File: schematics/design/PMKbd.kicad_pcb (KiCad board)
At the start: 2 copper layers, 28.4 x 53 mm, 84 parts, among them J1 Conn_01x01, J10 Conn_01x01, J11 Conn_01x01, J12 Conn_01x01, J13 Conn_01x01, J14 Conn_01x01, J15 Conn_01x01, J16 Conn_01x01, J17 Conn_01x01, J18 Conn_01x01, J19 Conn_01x01, J2 Conn_01x01, J20 Conn_01x01, J21 Conn_01x01, J22 Conn_01x01, J23 Conn_01x01, J24 Conn_01x01, J25 Conn_01x01, J26 Conn_01x01, J27 Conn_01x01, J28 Conn_01x01, J29 Conn_01x01, J3 Conn_01x01, J30 Conn_01x01, J31 Conn_01x01, J32 Conn_01x01, J33 Conn_01x01, J34 Conn_01x01, J35 Conn_01x01, J36 Conn_01x01, J37 Conn_01x01, J38 Conn_01x01, J39 Conn_01x01, J4 Conn_01x01, J40 Conn_01x01, J41 Conn_01x01, J42 Conn_01x01, J43 Conn_01x01, J44 Conn_01x01, J45 Conn_01x01, J46 Conn_01x01, J47 Conn_01x01, J48 Conn_01x01, J49 Conn_01x01, J5 Conn_01x01, J50 Conn_01x01, J51 Conn_01x01, J52 Conn_01x01, J53 Conn_01x01, J54 Conn_01x01, J55 Conn_01x01, J56 Conn_01x01, J57 Conn_01x01, J58 Conn_01x01, J59 Conn_01x01, J6 Conn_01x01, J60 Conn_01x01, J61 Conn_01x01, J62 Conn_01x01, J63 Conn_01x01, J64 Conn_01x01, J65 Conn_01x01, J66 Conn_01x01, J7 Conn_01x01, J8 Conn_01x01, J9 Conn_01x01, Q1 2N2222, Q2 2N2222, U1 Core51822_(B), U2 LT1117-3.3, U3 MCP73831-2-OT, U4 Core51822_(B), U5 MCP73831-2-OT, U6 LT1117-3.3

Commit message: fixed references
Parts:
- added J67: Conn_01x01, Connector_Wire:SolderWirePad_1x01_SMD_1x2mm, B.Cu at (151.8, 15.4)
- added J68: Conn_01x01, Connector_Wire:SolderWirePad_1x01_SMD_1x2mm, B.Cu at (162.8, 29.6)
- added J69: Conn_01x01, Connector_Wire:SolderWirePad_1x01_SMD_1x2mm, B.Cu at (153.0, 11.8)
- added J70: Conn_01x01, Connector_Wire:SolderWirePad_1x01_SMD_1x2mm, B.Cu at (172.3, 10.7)
- added J71: Conn_01x01, Connector_Wire:SolderWirePad_1x01_SMD_1x2mm, B.Cu at (150.7, 9.84)
- added J72: Conn_01x01, Connector_Wire:SolderWirePad_1x01_SMD_1x2mm, B.Cu at (168.0, 18.4)
- added J73: Conn_01x01, Connector_Wire:SolderWirePad_1x01_SMD_1x2mm, B.Cu at (173.2, 35.1)
- added J74: Conn_01x01, Connector_Wire:SolderWirePad_1x01_SMD_1x2mm, B.Cu at (166.9, 34.7)
- J34, J35, J36, J37: moved to F.Cu
- R10: value 200 -> 10K
- R9: value 10K -> 200
- U5: value MCP73831-2-OT -> LT1117-3.3
- U6: value LT1117-3.3 -> MCP73831-2-OT
- moved J35 76.6 mm to (100.4, 85.6)
- moved J37 73.1 mm to (99.5, 79.1)
- moved J36 72.1 mm to (102.7, 82.7)
- moved J34 71.0 mm to (97.7, 84.7)
- moved U4 52.3 mm to (75.3, 12.6)
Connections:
- net +5V renamed 5V_L
- net 3.3V renamed 3.3V_L
- net GND renamed GND_L
- net LED renamed LED_L
- J34 pad 1: Net-(J34-Pad1) -> EXT1
- J35 pad 1: Net-(J35-Pad1) -> EXT2
- J36 pad 1: Net-(BT2-Pad1) -> EXT3
- J37 pad 1: GND_R -> EXT4
- J40 pad 1: GND_R -> S24
- J41 pad 1: GND_R -> S25
- J42 pad 1: GND_R -> S26
- J43 pad 1: GND_R -> S27
- J44 pad 1: S24 -> S28
- J45 pad 1: S25 -> S29
- J46 pad 1: S26 -> S30
- J47 pad 1: S27 -> S31
- J48 pad 1: S28 -> S32
- J49 pad 1: S29 -> S33
- J50 pad 1: S30 -> S34
- J51 pad 1: S31 -> S35
- J52 pad 1: S32 -> S36
- J53 pad 1: S33 -> S37
- J54 pad 1: S34 -> S38
- J55 pad 1: S35 -> S39
- J56 pad 1: S36 -> S40
- J57 pad 1: S37 -> S41
- J58 pad 1: S38 -> S42
- J59 pad 1: S39 -> S43
- J60 pad 1: S40 -> S44
- J61 pad 1: S41 -> S45
- J62 pad 1: S42 -> S46
- J63 pad 1: S43 -> Net-(BT2-Pad1)
- J64 pad 1: S44 -> GND_R
- J65 pad 1: S45 -> GND_R
- J66 pad 1: S46 -> Net-(J66-Pad1)
- R10 pad 1: Net-(J38-Pad1) -> LED_R
- R10 pad 2: 3.3V_R -> Net-(Q2-Pad2)
- R9 pad 1: LED_R -> Net-(J38-Pad1)
- R9 pad 2: Net-(Q2-Pad2) -> 3.3V_R
- U1 pad 26: Net-(U1-Pad26) -> EXT4
- U1 pad 3: Net-(U1-Pad3) -> EXT1
- U1 pad 4: Net-(U1-Pad4) -> EXT2
- U1 pad 6: Net-(U1-Pad6) -> EXT3
- U4 pad 26: Net-(U4-Pad26) -> EXT8
- U4 pad 3: Net-(U4-Pad3) -> EXT5
- U4 pad 31: Net-(J35-Pad1) -> Net-(J67-Pad1)
- U4 pad 32: Net-(J34-Pad1) -> Net-(J66-Pad1)
- U4 pad 4: Net-(U4-Pad4) -> EXT6
- U4 pad 6: Net-(U4-Pad6) -> EXT7
- U5 pad 1: Net-(R6-Pad2) -> GND_R
- U5 pad 2: GND_R -> 3.3V_R
- U5 pad 4: 5V_R -> (no net)
- U5 pad 5: Net-(R8-Pad2) -> (no net)
- U6 pad 1: GND_R -> Net-(R6-Pad2)
- U6 pad 2: 3.3V_R -> GND_R
- U6 pad 4: (no net) -> 5V_R

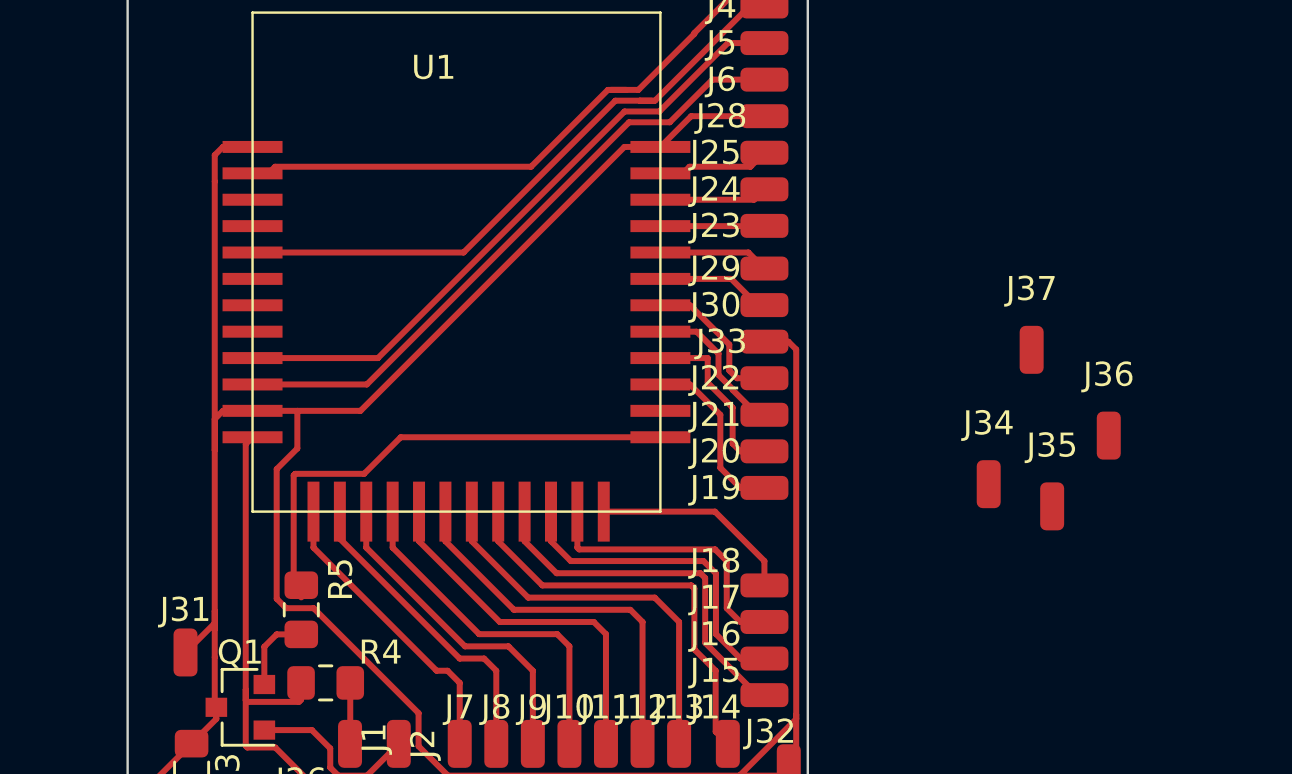
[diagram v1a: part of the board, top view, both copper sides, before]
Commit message: added EXT pads
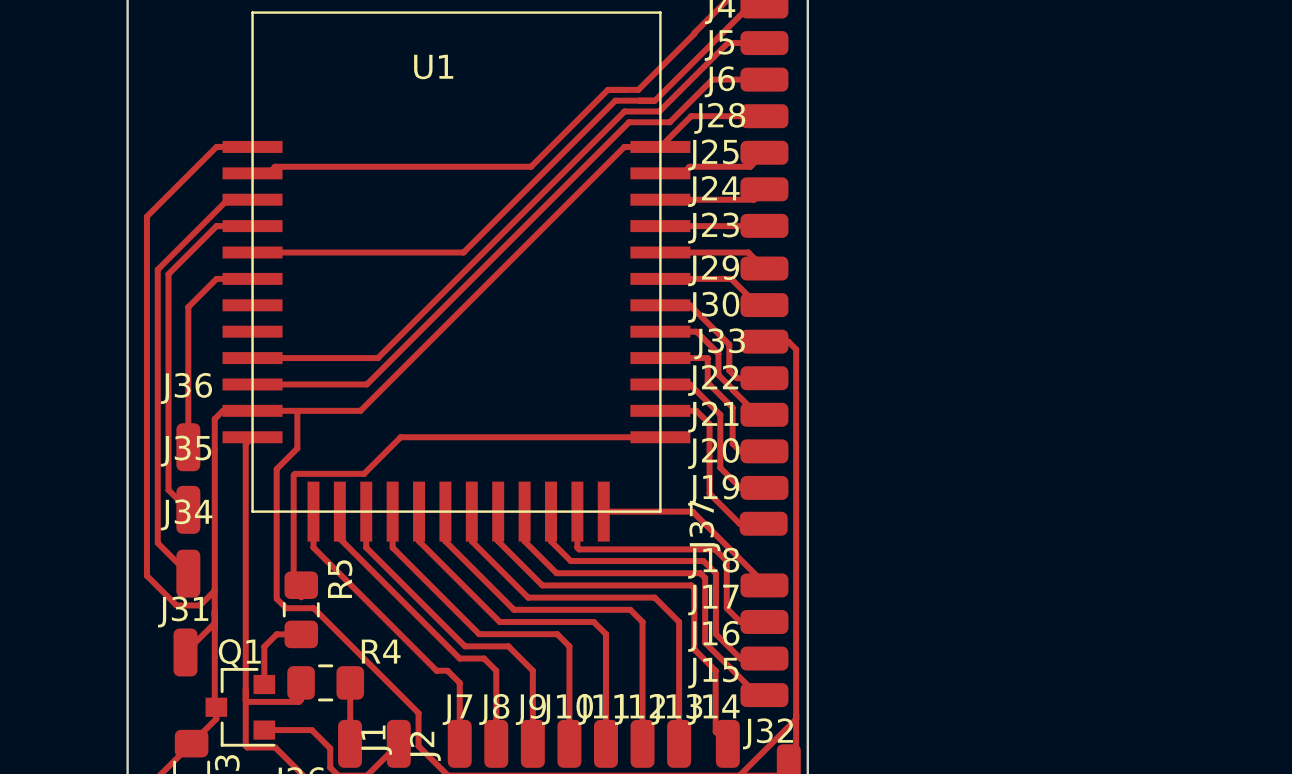
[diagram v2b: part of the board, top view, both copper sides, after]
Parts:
- moved J36 38.4 mm to (64.4, 83.1)
- moved J35 36.0 mm to (64.4, 85.8)
- moved J34 33.6 mm to (64.4, 88.4)
- moved J37 13.3 mm to (88.4, 86.3), turned to 90 degrees
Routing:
- net EXT1: track 0.00 -> 18.4 mm
- net EXT2: track 0.00 -> 14.5 mm
- net GND_L: track 145.0 -> 155.4 mm
- net EXT3: track 0.00 -> 9.00 mm
- net EXT4: track 0.00 -> 7.95 mm
- net S16: track 8.57 -> 8.02 mm
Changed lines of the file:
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@@
     (thickness 1.6)
     (drawings 6)
-    (tracks 243)
+    (tracks 264)
     (zones 0)
     (modules 92)
@@
   )
   (module Connector_Wire:SolderWirePad_1x01_SMD_1x2mm (layer F.Cu)
-    (at 99.53 79.08)
+    (at 88.36 86.33 90)
     (descr "Wire Pad, Square, SMD Pad,  5mm x 10mm,")
     (tags "MesurementPoint Square SMDPad 5mmx10mm ")
     (attr virtual)
-    (fp_text reference J37 (at 0 -2.54) (layer F.SilkS)
+    (fp_text reference J37 (at 0 -2.54 90) (layer F.SilkS)
       (effects (font (size 1 1) (thickness 0.15)))
     )
-    (fp_text value Conn_01x01 (at 0 2.54) (layer F.Fab)
+    (fp_text value Conn_01x01 (at 0 2.54 90) (layer F.Fab)
       (effects (font (size 1 1) (thickness 0.15)))
     )
@@
     (fp_line (start 0.63 1.27) (end 0.63 -1.27) (layer F.CrtYd) (width 0.05))
     (fp_line (start 0.63 -1.27) (end -0.63 -1.27) (layer F.CrtYd) (width 0.05))
-    (fp_text user %R (at 0 0) (layer F.Fab)
+    (fp_text user %R (at 0 0 90) (layer F.Fab)
       (effects (font (size 1 1) (thickness 0.15)))
     )
-    (pad 1 smd roundrect (at 0 0) (size 1 2) (layers F.Cu F.Paste F.Mask) (roundrect_rratio 0.25)
+    (pad 1 smd roundrect (at 0 0 90) (size 1 2) (layers F.Cu F.Paste F.Mask) (roundrect_rratio 0.25)
       (net 74 EXT4))
   )
   (module Connector_Wire:SolderWirePad_1x01_SMD_1x2mm (layer F.Cu)
-    (at 102.745 82.655)
+    (at 64.38 83.14)
     (descr "Wire Pad, Square, SMD Pad,  5mm x 10mm,")
     (tags "MesurementPoint Square SMDPad 5mmx10mm ")
@@
   )
   (module Connector_Wire:SolderWirePad_1x01_SMD_1x2mm (layer F.Cu)
-    (at 100.385 85.605)
+    (at 64.38 85.75)
     (descr "Wire Pad, Square, SMD Pad,  5mm x 10mm,")
     (tags "MesurementPoint Square SMDPad 5mmx10mm ")
@@
   )
   (module Connector_Wire:SolderWirePad_1x01_SMD_1x2mm (layer F.Cu)
-    (at 97.74 84.68)
+    (at 64.38 88.41)
     (descr "Wire Pad, Square, SMD Pad,  5mm x 10mm,")
     (tags "MesurementPoint Square SMDPad 5mmx10mm ")
@@
   (segment (start 65.820998 81.624) (end 65.480999 81.963999) (width 0.25) (layer F.Cu) (net 69))
   (segment (start 67.056 81.624) (end 65.820998 81.624) (width 0.25) (layer F.Cu) (net 69))
-  (segment (start 65.480999 70.963999) (end 65.480999 72.063999) (width 0.25) (layer F.Cu) (net 69))
-  (segment (start 67.056 70.624) (end 65.820998 70.624) (width 0.25) (layer F.Cu) (net 69))
-  (segment (start 65.820998 70.624) (end 65.480999 70.963999) (width 0.25) (layer F.Cu) (net 69))
   (segment (start 65.480999 81.963999) (end 65.480999 83.260999) (width 0.25) (layer F.Cu) (net 69))
-  (segment (start 65.480999 72.063999) (end 65.480999 83.260999) (width 0.25) (layer F.Cu) (net 69))
   (segment (start 65.548 94.463) (end 64.516 95.495) (width 0.25) (layer F.Cu) (net 69))
   (segment (start 65.548 93.98) (end 65.548 94.463) (width 0.25) (layer F.Cu) (net 69))
@@
   (segment (start 65.480999 90.626999) (end 65.480999 91.896999) (width 0.25) (layer F.Cu) (net 69))
   (segment (start 64.262 91.694) (end 65.480999 90.475001) (width 0.25) (layer F.Cu) (net 69))
-  (segment (start 65.480999 83.260999) (end 65.480999 89.967001) (width 0.25) (layer F.Cu) (net 69))
   (segment (start 65.480999 90.475001) (end 65.480999 89.967001) (width 0.25) (layer F.Cu) (net 69))
-  (segment (start 65.480999 89.967001) (end 65.480999 90.626999) (width 0.25) (layer F.Cu) (net 69))
   (segment (start 63.076999 102.192999) (end 63.076999 103.462999) (width 0.25) (layer F.Cu) (net 69))
   (segment (start 63.076999 103.462999) (end 62.156999 104.382999) (width 0.25) (layer F.Cu) (net 69))
@@
   (segment (start 88.382 73.924) (end 88.392 73.914) (width 0.25) (layer F.Cu) (net 25))
   (segment (start 84.056 73.924) (end 88.382 73.924) (width 0.25) (layer F.Cu) (net 25))
-  (segment (start 81.696 85.824) (end 86.332 85.824) (width 0.25) (layer F.Cu) (net 26))
-  (segment (start 88.392 87.884) (end 88.392 88.9) (width 0.25) (layer F.Cu) (net 26))
-  (segment (start 86.332 85.824) (end 88.392 87.884) (width 0.25) (layer F.Cu) (net 26))
+  (segment (start 88.392 88.817592) (end 88.392 88.9) (width 0.25) (layer F.Cu) (net 26))
+  (segment (start 85.398408 85.824) (end 88.392 88.817592) (width 0.25) (layer F.Cu) (net 26))
+  (segment (start 81.696 85.824) (end 85.398408 85.824) (width 0.25) (layer F.Cu) (net 26))
   (segment (start 85.291002 77.224) (end 84.056 77.224) (width 0.25) (layer F.Cu) (net 27))
   (segment (start 86.928019 78.861017) (end 85.291002 77.224) (width 0.25) (layer F.Cu) (net 27))
@@
   (segment (start 87.01081 76.124) (end 88.10281 77.216) (width 0.25) (layer F.Cu) (net 33))
   (segment (start 84.056 76.124) (end 87.01081 76.124) (width 0.25) (layer F.Cu) (net 33))
+  (segment (start 65.480999 89.967001) (end 65.480999 90.150999) (width 0.25) (layer F.Cu) (net 69))
+  (segment (start 65.480999 90.150999) (end 65.480999 90.626999) (width 0.25) (layer F.Cu) (net 69))
+  (segment (start 65.480999 89.122191) (end 65.480999 89.040999) (width 0.25) (layer F.Cu) (net 69))
+  (segment (start 64.86818 89.73501) (end 65.480999 89.122191) (width 0.25) (layer F.Cu) (net 69))
+  (segment (start 62.654971 73.525029) (end 62.654971 88.498161) (width 0.25) (layer F.Cu) (net 69))
+  (segment (start 63.89182 89.73501) (end 64.86818 89.73501) (width 0.25) (layer F.Cu) (net 69))
+  (segment (start 62.654971 88.498161) (end 63.89182 89.73501) (width 0.25) (layer F.Cu) (net 69))
+  (segment (start 65.556 70.624) (end 62.654971 73.525029) (width 0.25) (layer F.Cu) (net 69))
+  (segment (start 67.056 70.624) (end 65.556 70.624) (width 0.25) (layer F.Cu) (net 69))
+  (segment (start 65.480999 89.040999) (end 65.480999 90.150999) (width 0.25) (layer F.Cu) (net 69))
+  (segment (start 65.480999 83.260999) (end 65.480999 89.040999) (width 0.25) (layer F.Cu) (net 69))
+  (segment (start 63.10498 87.13498) (end 64.38 88.41) (width 0.25) (layer F.Cu) (net 71))
+  (segment (start 63.10498 75.73861) (end 63.10498 87.13498) (width 0.25) (layer F.Cu) (net 71))
+  (segment (start 66.01959 72.824) (end 63.10498 75.73861) (width 0.25) (layer F.Cu) (net 71))
+  (segment (start 67.056 72.824) (end 66.01959 72.824) (width 0.25) (layer F.Cu) (net 71))
+  (segment (start 63.55499 84.92499) (end 64.38 85.75) (width 0.25) (layer F.Cu) (net 72))
+  (segment (start 65.556 73.924) (end 63.55499 75.92501) (width 0.25) (layer F.Cu) (net 72))
+  (segment (start 63.55499 75.92501) (end 63.55499 84.92499) (width 0.25) (layer F.Cu) (net 72))
+  (segment (start 67.056 73.924) (end 65.556 73.924) (width 0.25) (layer F.Cu) (net 72))
+  (segment (start 65.556 76.124) (end 64.38 77.3) (width 0.25) (layer F.Cu) (net 73))
+  (segment (start 64.38 77.3) (end 64.38 83.14) (width 0.25) (layer F.Cu) (net 73))
+  (segment (start 67.056 76.124) (end 65.556 76.124) (width 0.25) (layer F.Cu) (net 73))
+  (segment (start 87.36 86.33) (end 88.36 86.33) (width 0.25) (layer F.Cu) (net 74))
+  (segment (start 86.104992 85.074992) (end 87.36 86.33) (width 0.25) (layer F.Cu) (net 74))
+  (segment (start 86.104992 82.172992) (end 86.104992 85.074992) (width 0.25) (layer F.Cu) (net 74))
+  (segment (start 85.556 81.624) (end 86.104992 82.172992) (width 0.25) (layer F.Cu) (net 74))
+  (segment (start 84.056 81.624) (end 85.556 81.624) (width 0.25) (layer F.Cu) (net 74))
 )

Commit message: optimized, missing lib added
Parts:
- moved J69 119.6 mm to (250.9, 80.4)
- moved R8 117.5 mm to (186.3, 114.8)
- moved R9 117.5 mm to (181.5, 114.8)
- moved J38 113.0 mm to (212.3, 106.4)
- moved J39 113.0 mm to (217.9, 111.4)
- moved J65 104.7 mm to (232.7, 85.5)
- moved C3 103.9 mm to (159.8, 109.0), turned to 180 degrees
- moved U4 100.9 mm to (157.3, 71.4)
- moved J63 97.5 mm to (227.1, 102.1)
- moved J64 97.5 mm to (224.4, 98.4)
- moved Q2 93.0 mm to (180.4, 109.3)
- moved R10 84.3 mm to (205.1, 91.7)
- moved J46 82.5 mm to (146.5, 99.9)
- moved U6 82.2 mm to (158.5, 116.4), turned to 270 degrees
- moved J51 81.2 mm to (139.0, 100.0)
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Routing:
- net GND_R: track 0.00 -> 51.9 mm
- net S26: track 0.00 -> 26.1 mm
- net S27: track 0.00 -> 25.9 mm
- net S25: track 0.00 -> 24.9 mm
- net S24: track 0.00 -> 24.1 mm
- net S35: track 0.00 -> 12.8 mm
- net S36: track 0.00 -> 12.7 mm
- net S33: track 0.00 -> 12.7 mm
- net S34: track 0.00 -> 12.5 mm
- net S32: track 0.00 -> 12.2 mm
- net S31: track 0.00 -> 11.7 mm
- net S30: track 0.00 -> 11.6 mm
- net S28: track 0.00 -> 11.6 mm
- net S29: track 0.00 -> 11.4 mm
- net S37: track 0.00 -> 10.7 mm
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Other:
- board size 28.4 x 53 mm -> 28.2 x 53.1 mm

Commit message: optimized more
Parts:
- moved J34 16.2 mm to (64.5, 72.2)
- moved J35 10.3 mm to (64.5, 75.4)
- moved R3 9.69 mm to (65.9, 86.9), turned to 0 degrees
- moved U3 9.48 mm to (64.3, 90.7), turned to 270 degrees
- moved C2 8.97 mm to (64.3, 96.5), turned to 180 degrees
- moved U2 8.72 mm to (66.1, 102.3)
- moved C1 8.68 mm to (64.2, 94.3), turned to 0 degrees
- moved J31 7.45 mm to (64.8, 84.3)
- moved J27 7.05 mm to (68.8, 96.5), turned to 180 degrees
- moved J36 4.15 mm to (64.5, 79.0)
- moved J26 2.41 mm to (67.3, 96.6)
- moved J1 1.65 mm to (72.6, 94.5)
- moved R4 1.59 mm to (71.6, 92.3)
- moved R5 1.56 mm to (70.6, 90.2), turned to 0 degrees
- moved Q1 1.49 mm to (67.7, 93.0)
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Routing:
- net GND_L: track 160.9 -> 99.7 mm
- net EXT1: track 18.4 -> 2.80 mm
- net EXT2: track 14.5 -> 3.17 mm
- net 3.3V_L: track 33.8 -> 27.2 mm
- net EXT3: track 9.00 -> 4.53 mm
- net Net-(J2-Pad1): track 10.6 -> 7.15 mm
- net Net-(Q1-Pad2): track 3.33 -> 6.28 mm
- net Net-(R3-Pad2): track 3.02 -> 5.81 mm
- net Net-(BT1-Pad1): track 13.6 -> 16.1 mm
- net S5: track 11.5 -> 13.2 mm
- net LED_L: track 21.1 -> 22.0 mm
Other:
- board size 28.2 x 53.1 mm -> 28.1 x 44.6 mm

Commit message: minor changes
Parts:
- moved C2 8.39 mm to (72.3, 99.1), turned to 270 degrees
- moved J27 7.44 mm to (75.9, 98.5)
- moved J26 7.36 mm to (74.4, 98.5)
- moved J1 7.16 mm to (79.2, 97.4)
- moved J2 4.55 mm to (77.7, 97.4)
- moved U2 4.01 mm to (66.4, 98.3), turned to 180 degrees
- moved R4 0.76 mm to (72.1, 92.8)
- moved R5 0.68 mm to (70.1, 89.8)
- moved C1 0.46 mm to (64.3, 93.9)
- moved Q1 0.37 mm to (67.9, 92.7)
- moved U3 0.34 mm to (64.4, 90.4)
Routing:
- net GND_L: track 99.7 -> 110.3 mm
- net Net-(J1-Pad1): track 2.18 -> 12.2 mm
- net Net-(BT1-Pad1): track 16.1 -> 25.5 mm
- net 3.3V_L: track 27.2 -> 22.5 mm
- net Net-(J2-Pad1): track 7.15 -> 10.3 mm
- net Net-(Q1-Pad2): track 6.28 -> 3.47 mm
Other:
- board size 28.1 x 44.6 mm -> 28.1 x 39.6 mm
